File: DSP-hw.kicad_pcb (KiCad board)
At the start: 2 copper layers, 185 x 66.6 mm, 118 parts, among them J1 NC3MAH, J10 AudioJack3, J11 AudioJack3, J2 NC3MAH, J3 NC3MAH, J4 NC3MAH, J5 XLR3_AudioJack3_Combo_Ground, J6 XLR3_AudioJack3_Combo_Ground, J7 USB_C_Receptacle_USB2.0_16P, J8 Conn_01x04_Pin, J9 Conn_01x06_Pin, Q1 BC327, Q2 AO3400A, SW1 SW_Push, SW2 SW_Push, SW6 SW_SPST, SW7 SW_SPST, SW8 SW_Push, U1 ADAU1701, U2 CAT24C256, U3 AMS1117-3.3, U4 STM32F411RETx, U5 TME-0505S, U6 ADUM3160, Y1 12.228M, Y2 Crystal_GND24

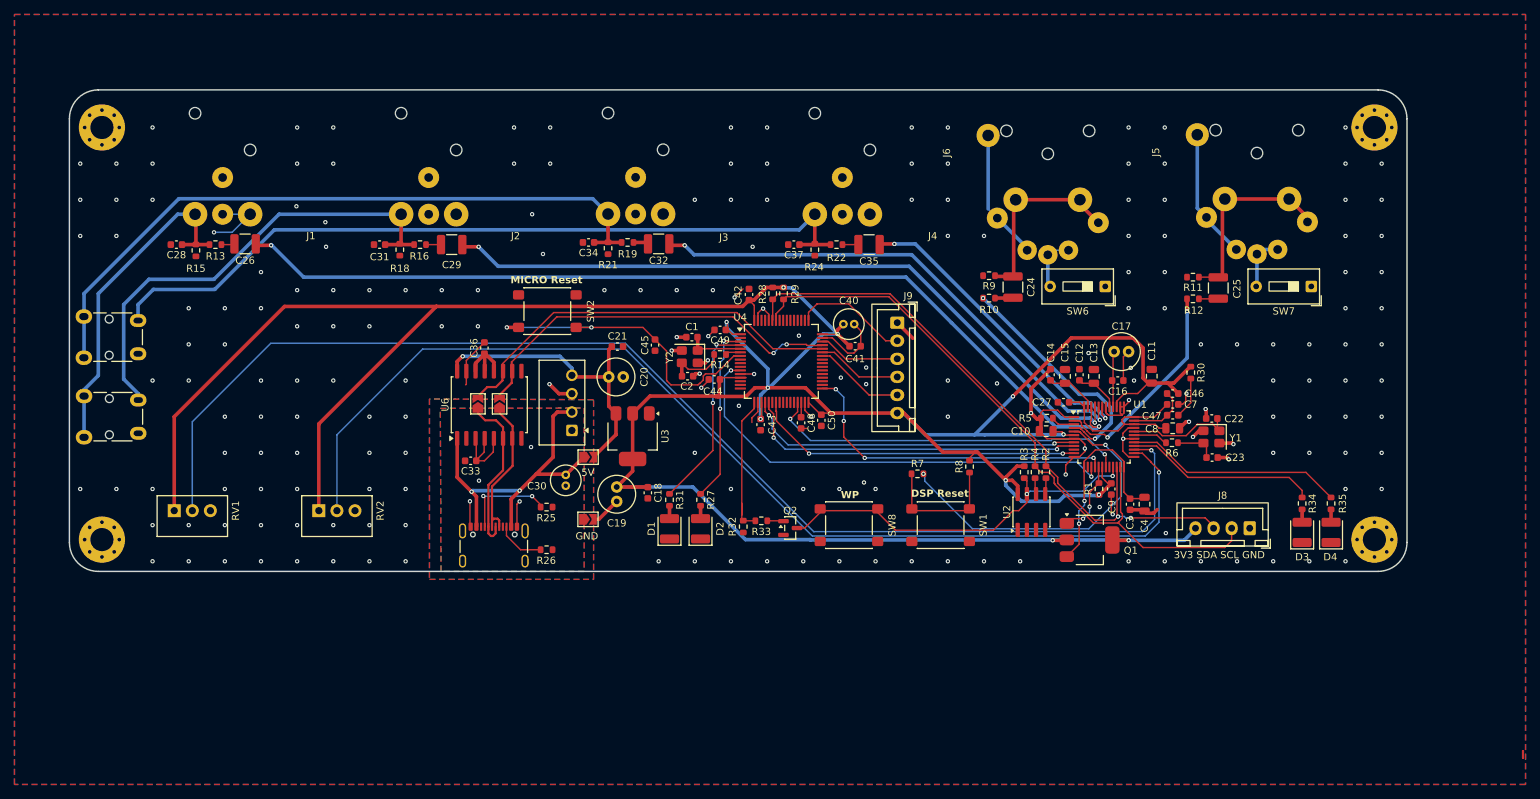
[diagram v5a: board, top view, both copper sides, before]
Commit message: messa apposto la silkscreen
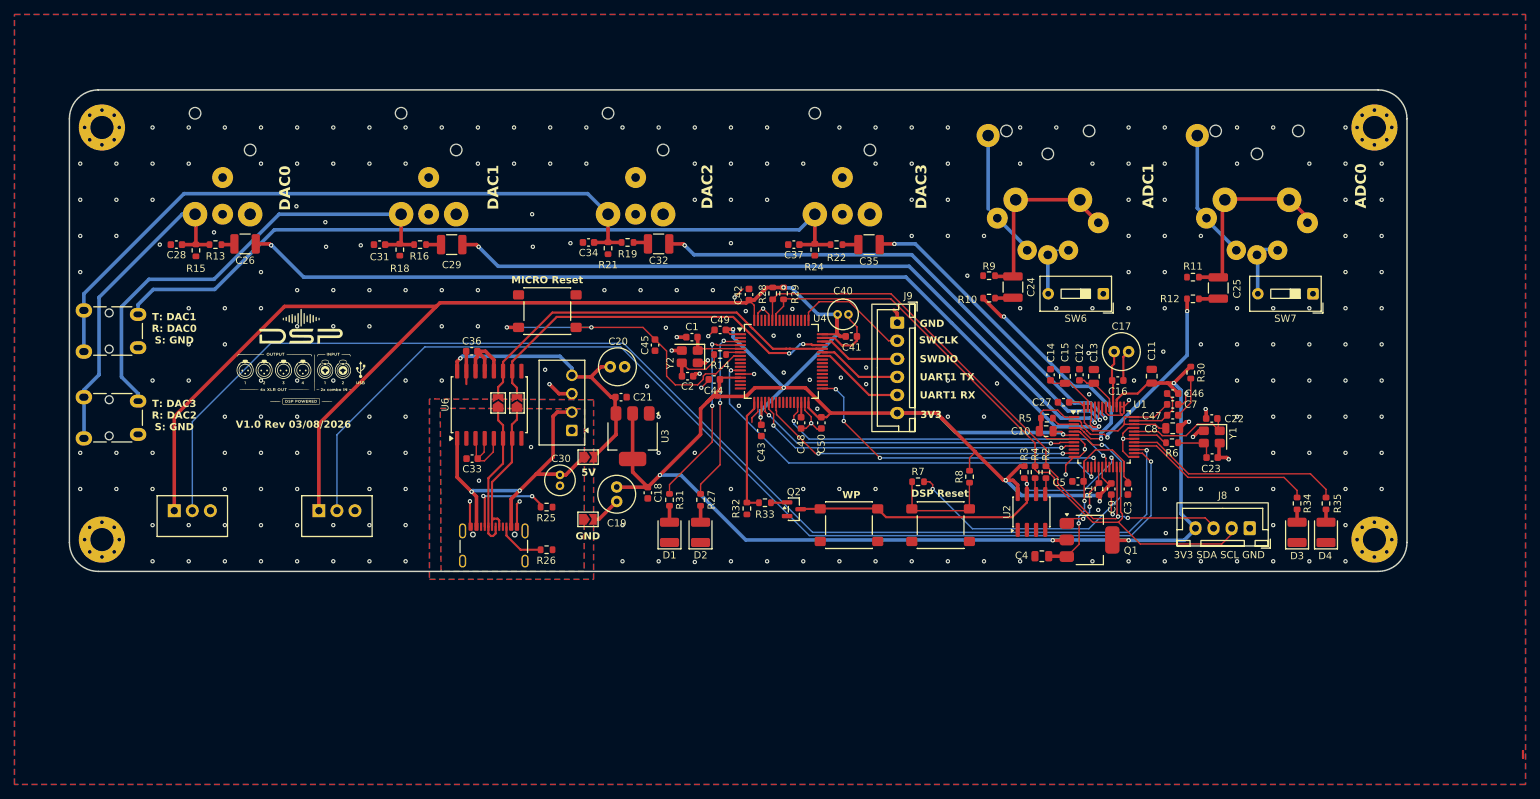
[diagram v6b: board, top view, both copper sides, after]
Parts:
- added C5: 100n, Capacitor_SMD:C_0603_1608Metric, F.Cu at (198.0, 83.9)
- added G***: LOGO, LOGO, F.Cu at (90.5, 66.7)
- moved C4 15.9 mm to (193.0, 94.3), turned to 180 degrees
- moved C21 7.02 mm to (134.8, 72.3)
- moved JP2 2.80 mm to (117.8, 73.1)
- moved Q2 2.65 mm to (158.7, 87.8)
- moved R32 2.55 mm to (152.2, 87.7)
- moved R33 2.55 mm to (154.7, 86.9)
- moved JP3 2.40 mm to (120.4, 73.1)
- moved C3 2.13 mm to (204.9, 85.0)
- moved C36 1.81 mm to (114.2, 66.0), turned to 180 degrees
- moved C40 1.57 mm to (164.8, 60.9)
- moved C41 1.45 mm to (166.7, 63.9)
- moved C20 1.41 mm to (133.3, 68.1)
- moved R8 1.40 mm to (183.0, 83.3)
- moved R7 1.10 mm to (175.9, 84.0)
- moved SW6 1.05 mm to (201.5, 58.0)
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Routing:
- net GND: track 126.4 -> 102.7 mm, vias 204 -> 271
- net +3V3: track 473.9 -> 464.0 mm
- net /WP_M: track 20.4 -> 15.9 mm
- net Net-(R7-Pad1): track 18.4 -> 15.5 mm
- net /MP8: track 173.6 -> 171.3 mm
- net +5V: track 41.5 -> 39.3 mm
- net Net-(Q1-C): track 28.6 -> 26.6 mm
- net Net-(U6-PIN): track 8.40 -> 10.4 mm
- net /DOUT: track 63.8 -> 61.8 mm
- net /Micro/D-: track 22.6 -> 20.7 mm
- net /MP9: track 152.2 -> 150.4 mm
- net Net-(SW7-B): track 7.64 -> 9.44 mm
- net Net-(SW6-B): track 7.63 -> 9.01 mm
- net /Micro/D- iso: track 56.2 -> 54.9 mm
- net /BCLK_1: track 47.7 -> 46.5 mm
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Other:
- board text added: "3V3"
- board text added: "ADC0"
- board text added: "ADC1"
- board text added: "DAC0"
- board text added: "DAC1"
- board text added: "DAC2"
- board text added: "DAC3"
- board text added: "SWCLK"
- board text added: "SWDIO"
- board text added: "T: DAC1 R: DAC0 S: GND"
- board text added: "T: DAC3 R: DAC2 S: GND"
- board text added: "UART1 RX"
- board text added: "UART1 TX"
- board text added: "V1.0 Rev 03/08/2026"

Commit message: bom completata
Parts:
- C1, C2: value 12p -> 18p
- C24, C25, C26, C29, C32, C35: footprint Capacitor_SMD:C_1210_3225Metric -> Capacitor_SMD:C_0805_2012Metric
- C48: footprint Capacitor_SMD:C_0603_1608Metric -> Capacitor_THT:C_Radial_D4.0mm_H7.0mm_P1.50mm
- J10, J11: footprint Connector_Audio:Jack_3.5mm_Lumberg_1503_07_Horizontal -> Connector_Audio:Jack_3.5mm_CUI_SJ1-3523N_Horizontal
- Q1: value BC327 -> BCX52; footprint Package_TO_SOT_SMD:SOT-223-3_TabPin2 -> Package_TO_SOT_SMD:SOT-89-3
- Y2: value Crystal_GND24 -> 8M
- moved C4 6.31 mm to (195.6, 88.5), turned to -90 degrees
- moved C48 5.79 mm to (165.4, 76.5), turned to 0 degrees
- moved J11 4.64 mm to (63.0, 62.1), turned to -90 degrees
- moved J10 4.11 mm to (63.0, 74.7), turned to -90 degrees
- moved Q1 2.02 mm to (198.1, 93.3), turned to -90 degrees
- moved C50 1.00 mm to (161.9, 75.0), turned to 0 degrees
- moved C44 0.40 mm to (148.1, 69.8)
- moved R18 0.18 mm to (104.3, 52.0)
- moved C25 0.16 mm to (217.6, 57.1)
- moved C31 0.15 mm to (101.5, 51.2)
- moved C37 0.13 mm to (158.8, 51.1)
- moved R25 0.10 mm to (124.5, 87.4)
- moved C34 0.05 mm to (130.3, 51.0)
- moved R24 0.05 mm to (161.6, 52.0)
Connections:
- C3 pad 1: Net-(Q1-C) -> Net-(Q1-E)
- C4 pad 1: Net-(Q1-C) -> Net-(Q1-E)
- C5 pad 1: Net-(Q1-C) -> Net-(Q1-E)
- Q1 pad 1: Net-(Q1-C) -> Net-(Q1-B)
- Q1 pad 2: Net-(Q1-B) -> +3V3
- Q1 pad 3: +3V3 -> Net-(Q1-E)
- U1 pad 13: Net-(Q1-C) -> Net-(Q1-E)
- U1 pad 24: Net-(Q1-C) -> Net-(Q1-E)
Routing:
- net Net-(Q1-C): track 26.6 -> 0.00 mm, vias 2 -> 0
- net Net-(Q1-E): track 0.00 -> 24.2 mm, vias 0 -> 2
- net GNDA: track 7.21 -> 22.1 mm, vias 4 -> 8
- net Net-(U4-VCAP1): track 2.15 -> 8.80 mm
- net GND: track 102.7 -> 105.5 mm, vias 271 -> 290
- net Net-(C37-Pad1): track 108.5 -> 106.2 mm
- net Net-(J7-CC1): track 13.5 -> 11.5 mm
- net Net-(C31-Pad1): track 66.0 -> 64.4 mm
- net Net-(C28-Pad1): track 46.3 -> 47.7 mm
- net /LRCK_2: track 44.8 -> 45.6 mm
- net +3V3: track 464.0 -> 464.8 mm, vias 11 -> 10
- net Net-(C34-Pad1): track 95.1 -> 95.8 mm, vias 0 -> 1
- net Net-(U1-~{RESET}): track 45.3 -> 44.7 mm
- net /ADC1: track 33.2 -> 32.7 mm
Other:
- outline, holes or cut-outs redrawn
- board text added: "MP2"
- board text added: "MP3"
- board text added: "PC14"
- board text added: "PC15"
